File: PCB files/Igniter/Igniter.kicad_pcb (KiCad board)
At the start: 2 copper layers, 124.9 x 69.6 mm, 56 parts, among them IC1 74HC4050, J1 PT, J10 SL3, J11 SL4, J12 SL5, J13 Micro_SD_Card, J2 PT, J3 PT, J4 PT, J5 Battery, J6 Ignition Coil +, J7 Ignition coil -, J8 SL1, J9 SL2, Q1 N MOSFET, Q2 N MOSFET, Q3 N MOSFET, Q4 N MOSFET, Q5 N MOSFET, Q6 N MOSFET, SW1 ARM, U2 FDS8984, U3 FDS8984, U4 FDS8984

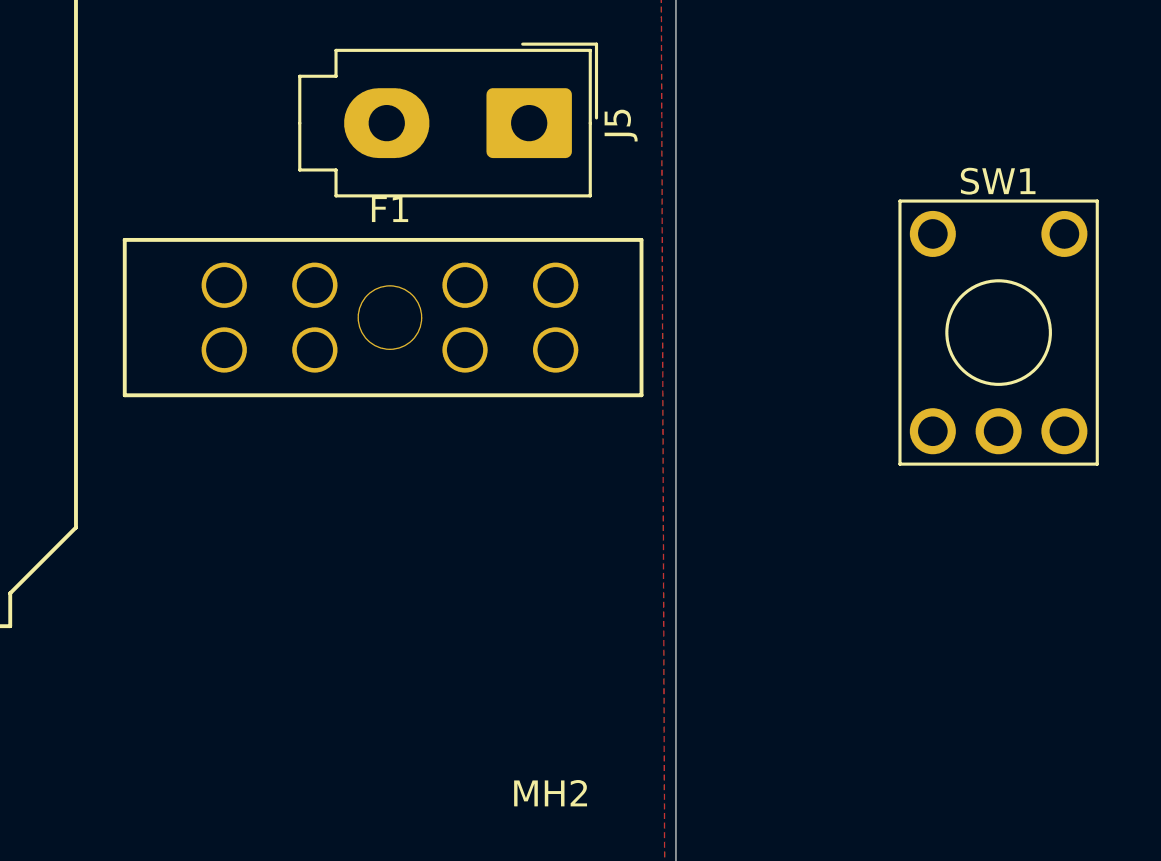
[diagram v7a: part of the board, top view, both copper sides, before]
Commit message: 1/9/2020
-Added C&K switch footprint to board
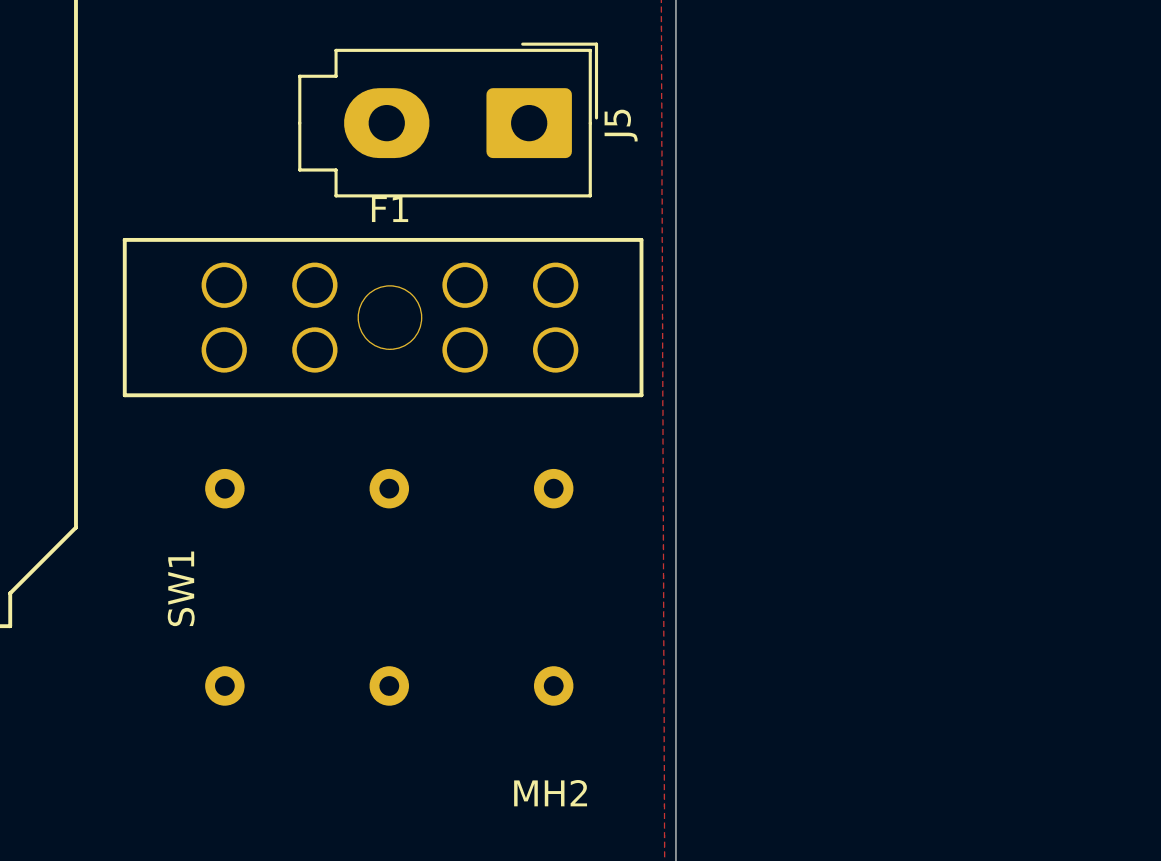
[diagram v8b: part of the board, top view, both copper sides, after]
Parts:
- SW1: footprint Button_Switch_THT:KSA_Tactile_SPST -> IgniterFootprints:C&K_S101031MS02Q
- moved SW1 25.1 mm to (198.9, 138.2), turned to 90 degrees
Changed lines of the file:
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@@
     )
   )
-  (module Button_Switch_THT:KSA_Tactile_SPST (layer F.Cu)
-    (at 219.92844 124.48032)
-    (descr "KSA http://www.ckswitches.com/media/1457/ksa_ksl.pdf")
-    (tags "SWITCH SMD KSA SW")
-    (fp_text reference SW1 (at 2.54 -2) (layer F.SilkS)
+  (module IgniterFootprints:C&K_S101031MS02Q (layer F.Cu)
+    (at 198.93534 138.16838 90)
+    (fp_text reference SW1 (at 0 -8 90) (layer F.SilkS)
       (effects (font (size 1 1) (thickness 0.15)))
     )
-    (fp_text value ARM (at 2.54 10) (layer F.Fab)
+    (fp_text value ARM (at 0 8.5 90) (layer F.Fab)
       (effects (font (size 1 1) (thickness 0.15)))
     )
-    (fp_line (start -1.16 7.91) (end 6.24 7.91) (layer F.Fab) (width 0.1))
-    (fp_line (start 6.24 -0.29) (end -1.16 -0.29) (layer F.Fab) (width 0.1))
-    (fp_line (start -1.16 7.91) (end -1.16 -0.29) (layer F.Fab) (width 0.1))
-    (fp_text user %R (at 2.54 4) (layer F.Fab)
-      (effects (font (size 1 1) (thickness 0.15)))
-    )
-    (fp_line (start 6.35 8.89) (end 6.35 -1.27) (layer F.SilkS) (width 0.12))
-    (fp_line (start -1.27 -1.27) (end 6.35 -1.27) (layer F.SilkS) (width 0.12))
-    (fp_line (start -1.27 -1.27) (end -1.27 8.89) (layer F.SilkS) (width 0.12))
-    (fp_line (start -1.27 8.89) (end 6.35 8.89) (layer F.SilkS) (width 0.12))
-    (fp_line (start -1.41 -1.14) (end 6.49 -1.14) (layer F.CrtYd) (width 0.05))
-    (fp_line (start -1.41 -1.14) (end -1.41 8.75) (layer F.CrtYd) (width 0.05))
-    (fp_line (start 6.49 8.75) (end 6.49 -1.14) (layer F.CrtYd) (width 0.05))
-    (fp_line (start 6.49 8.75) (end -1.41 8.75) (layer F.CrtYd) (width 0.05))
-    (fp_circle (center 2.54 3.81) (end 0.54 3.81) (layer F.SilkS) (width 0.12))
-    (fp_line (start 6.24 7.91) (end 6.24 -0.29) (layer F.Fab) (width 0.1))
-    (pad 1 thru_hole circle (at 0 0) (size 1.778 1.778) (drill 1.143) (layers *.Cu *.Mask)
+    (pad 1 thru_hole circle (at -3.77 -6.35 90) (size 1.524 1.524) (drill 0.762) (layers *.Cu *.Mask)
       (net 109 "Net-(J5-Pad1)"))
-    (pad 2 thru_hole circle (at 5.08 0) (size 1.778 1.778) (drill 1.143) (layers *.Cu *.Mask)
+    (pad 2 thru_hole circle (at 3.85 -6.35 90) (size 1.524 1.524) (drill 0.762) (layers *.Cu *.Mask)
       (net 24 "Net-(F1-Pad5)"))
-    (pad 3 thru_hole circle (at 5.08 7.62) (size 1.778 1.778) (drill 1.143) (layers *.Cu *.Mask))
-    (pad 4 thru_hole circle (at 2.54 7.62) (size 1.778 1.778) (drill 1.143) (layers *.Cu *.Mask))
-    (pad 5 thru_hole circle (at 0 7.62) (size 1.778 1.778) (drill 1.143) (layers *.Cu *.Mask))
-    (model ${KISYS3DMOD}/Button_Switch_THT.3dshapes/KSA_Tactile_SPST.wrl
-      (at (xyz 0 0 0))
-      (scale (xyz 1 1 1))
-      (rotate (xyz 0 0 0))
-    )
+    (pad 3 thru_hole circle (at -3.77 0 90) (size 1.524 1.524) (drill 0.762) (layers *.Cu *.Mask))
+    (pad 4 thru_hole circle (at 3.85 0 90) (size 1.524 1.524) (drill 0.762) (layers *.Cu *.Mask))
+    (pad 5 thru_hole circle (at -3.77 6.35 90) (size 1.524 1.524) (drill 0.762) (layers *.Cu *.Mask))
+    (pad 6 thru_hole circle (at 3.85 6.35 90) (size 1.524 1.524) (drill 0.762) (layers *.Cu *.Mask))
   )
   (gr_text "PT1\n" (at 98.91268 153.55316) (layer F.SilkS)
